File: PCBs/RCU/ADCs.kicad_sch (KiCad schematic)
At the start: 18 parts

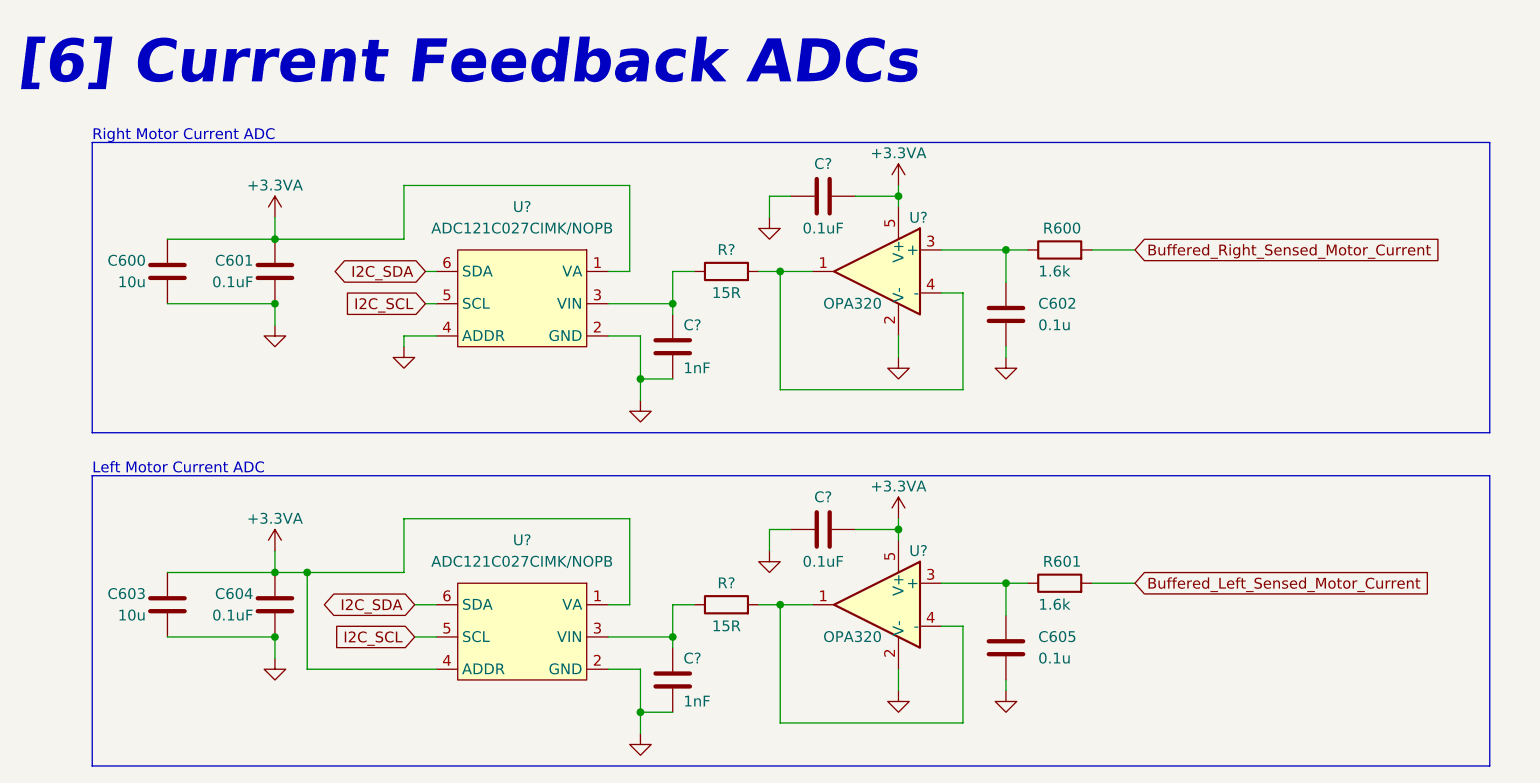
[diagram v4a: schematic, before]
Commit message: Fully annotated ADC schematic
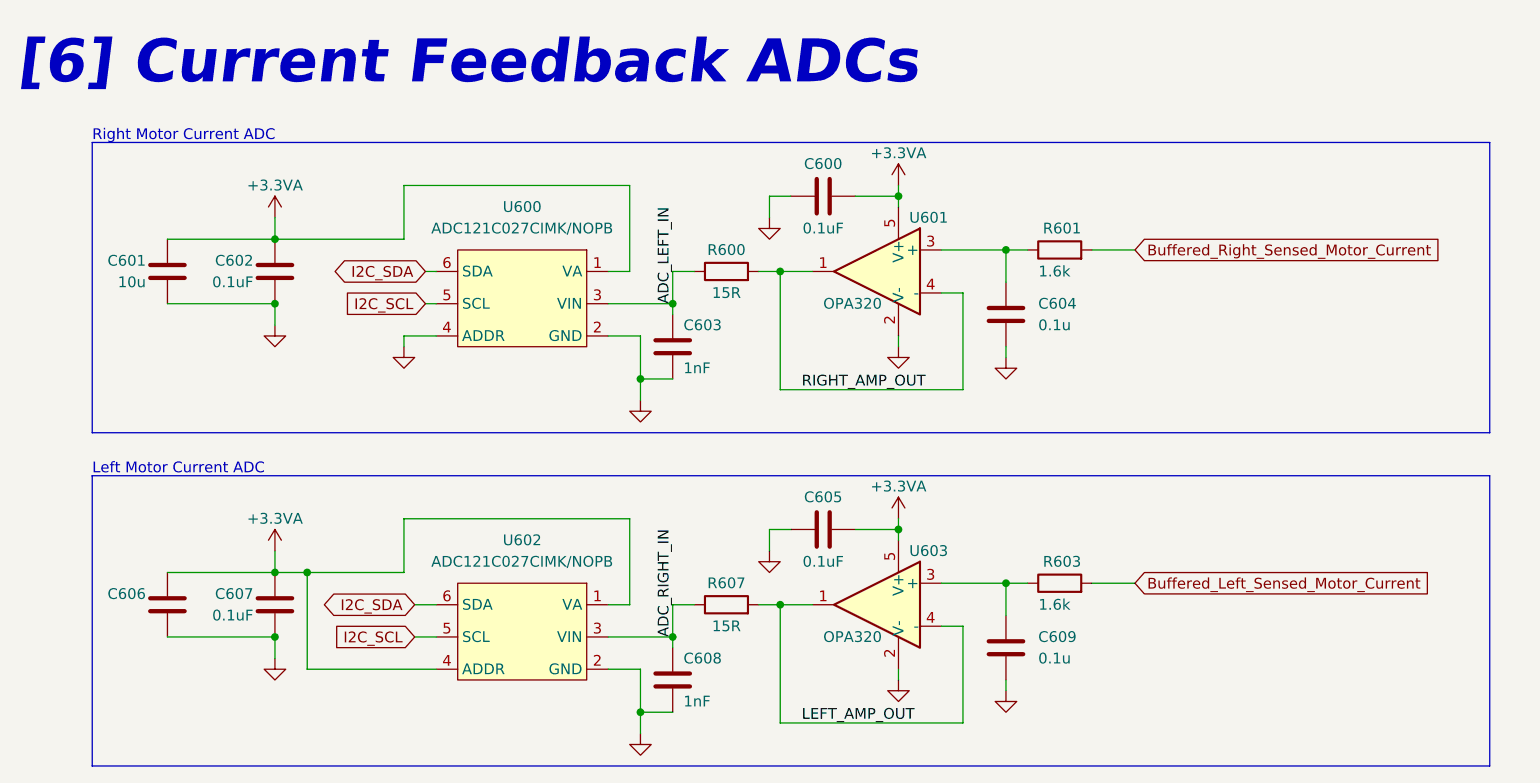
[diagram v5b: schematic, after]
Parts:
- C606: renamed from C603; value 10u -> (none)
- gave numbers to parts that had none: 10
- renumbered C600 to C601, C601 to C602, C602 to C604, C604 to C607, C605 to C609, R600 to R601, R601 to R603
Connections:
- net RIGHT_AMP_OUT: now reaches R600.2, U601.1, U601.4 (-)
- net ADC_RIGHT_IN: now reaches C608.1, R607.1, U602.3 (VIN)
- net ADC_LEFT_IN: now reaches C603.1, R600.1, U600.3 (VIN)
- net LEFT_AMP_OUT: now reaches R607.2, U603.1, U603.4 (-)
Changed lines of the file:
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@@
   (junction (at 105.41 83.82) (diameter 0) (color 0 0 0 0)
   )
-  (wire (pts (xy 119.38 91.44) (xy 119.38 93.98))
+  (wire (pts (xy 119.38 91.44) (xy 119.38 92.71))
     (stroke (width 0) (type default) (color 0 0 0 0))
   )
@@
     (stroke (width 0) (type default) (color 0 0 0 0))
   )
-  (wire (pts (xy 119.38 52.07) (xy 119.38 54.61))
+  (wire (pts (xy 119.38 52.07) (xy 119.38 53.34))
     (stroke (width 0) (type default) (color 0 0 0 0))
   )
@@
   (text "[6] Current Feedback ADCs" (at 15.24 22.86 0)
     (effects (font (size 5.08 5.08) (thickness 1.016) bold italic) (justify left bottom))
+  )
+  (label "LEFT_AMP_OUT" (at 107.95 97.79 0)
+    (effects (font (size 1.27 1.27)) (justify left bottom))
+  )
+  (label "RIGHT_AMP_OUT" (at 107.95 58.42 0)
+    (effects (font (size 1.27 1.27)) (justify left bottom))
+  )
+  (label "ADC_RIGHT_IN" (at 92.71 87.63 90)
+    (effects (font (size 1.27 1.27)) (justify left bottom))
+  )
+  (label "ADC_LEFT_IN" (at 92.71 48.26 90)
+    (effects (font (size 1.27 1.27)) (justify left bottom))
   )
   (global_label "I2C_SCL" (shape input) (at 63.5 48.26 180) (fields_autoplaced)
@@
     )
   )
-  (symbol (lib_id "power:GND") (at 119.38 93.98 0) (unit 1)
-    (in_bom yes) (on_board yes) (fields_autoplaced)
-    (property "Reference" "#PWR?" (id 0) (at 119.38 100.33 0)
-      (effects (font (size 1.27 1.27)) hide)
-    )
-    (property "Value" "GND" (id 1) (at 119.38 99.06 0)
-      (effects (font (size 1.27 1.27)) hide)
-    )
-    (property "Footprint" "" (id 2) (at 119.38 93.98 0)
-      (effects (font (size 1.27 1.27)) hide)
-    )
-    (property "Datasheet" "" (id 3) (at 119.38 93.98 0)
+  (symbol (lib_id "power:GND") (at 119.38 92.71 0) (unit 1)
+    (in_bom yes) (on_board yes) (fields_autoplaced)
+    (property "Reference" "#PWR?" (id 0) (at 119.38 99.06 0)
+      (effects (font (size 1.27 1.27)) hide)
+    )
+    (property "Value" "GND" (id 1) (at 119.38 97.79 0)
+      (effects (font (size 1.27 1.27)) hide)
+    )
+    (property "Footprint" "" (id 2) (at 119.38 92.71 0)
+      (effects (font (size 1.27 1.27)) hide)
+    )
+    (property "Datasheet" "" (id 3) (at 119.38 92.71 0)
       (effects (font (size 1.27 1.27)) hide)
     )
@@
   (symbol (lib_id "Device:R") (at 138.43 41.91 90) (unit 1)
     (in_bom yes) (on_board yes)
-    (property "Reference" "R600" (id 0) (at 140.97 39.37 90)
+    (property "Reference" "R601" (id 0) (at 140.97 39.37 90)
       (effects (font (size 1.27 1.27)) (justify left))
     )
@@
   (symbol (lib_id "Device:C") (at 45.72 44.45 0) (mirror y) (unit 1)
     (in_bom yes) (on_board yes)
-    (property "Reference" "C601" (id 0) (at 43.18 43.18 0)
+    (property "Reference" "C602" (id 0) (at 43.18 43.18 0)
       (effects (font (size 1.27 1.27)) (justify left))
     )
@@
   (symbol (lib_id "Device:C") (at 132.08 88.9 180) (unit 1)
     (in_bom yes) (on_board yes) (fields_autoplaced)
-    (property "Reference" "C605" (id 0) (at 135.89 87.6299 0)
+    (property "Reference" "C609" (id 0) (at 135.89 87.6299 0)
       (effects (font (size 1.27 1.27)) (justify right))
     )
@@
   (symbol (lib_id "Amplifier_Operational:OPA330xxDBV") (at 116.84 44.45 0) (mirror y) (unit 1)
     (in_bom yes) (on_board yes)
-    (property "Reference" "U?" (id 0) (at 120.65 38.1 0)
+    (property "Reference" "U601" (id 0) (at 120.65 38.1 0)
       (effects (font (size 1.27 1.27)) (justify right))
     )
@@
   (symbol (lib_id "Device:C") (at 110.49 35.56 90) (unit 1)
     (in_bom yes) (on_board yes)
-    (property "Reference" "C?" (id 0) (at 110.49 31.75 90))
+    (property "Reference" "C600" (id 0) (at 110.49 31.75 90))
     (property "Value" "0.1uF" (id 1) (at 110.49 39.37 90))
     (property "Footprint" "" (id 2) (at 114.3 34.5948 0)
@@
   (symbol (lib_id "Device:C") (at 110.49 74.93 90) (unit 1)
     (in_bom yes) (on_board yes)
-    (property "Reference" "C?" (id 0) (at 110.49 71.12 90))
+    (property "Reference" "C605" (id 0) (at 110.49 71.12 90))
     (property "Value" "0.1uF" (id 1) (at 110.49 78.74 90))
     (property "Footprint" "" (id 2) (at 114.3 73.9648 0)
@@
   (symbol (lib_id "Device:C") (at 33.02 44.45 0) (mirror y) (unit 1)
     (in_bom yes) (on_board yes)
-    (property "Reference" "C600" (id 0) (at 30.48 43.18 0)
+    (property "Reference" "C601" (id 0) (at 30.48 43.18 0)
       (effects (font (size 1.27 1.27)) (justify left))
     )
@@
   (symbol (lib_id "Device:C") (at 92.71 92.71 0) (unit 1)
     (in_bom yes) (on_board yes)
-    (property "Reference" "C?" (id 0) (at 93.98 90.17 0)
+    (property "Reference" "C608" (id 0) (at 93.98 90.17 0)
       (effects (font (size 1.27 1.27)) (justify left))
     )
@@
   (symbol (lib_id "Device:R") (at 99.06 44.45 90) (unit 1)
     (in_bom yes) (on_board yes)
-    (property "Reference" "R?" (id 0) (at 99.06 41.91 90))
+    (property "Reference" "R600" (id 0) (at 99.06 41.91 90))
     (property "Value" "15R" (id 1) (at 99.06 46.99 90))
     (property "Footprint" "" (id 2) (at 99.06 46.228 90)
@@
   (symbol (lib_id "Device:C") (at 92.71 53.34 0) (unit 1)
     (in_bom yes) (on_board yes)
-    (property "Reference" "C?" (id 0) (at 93.98 50.8 0)
+    (property "Reference" "C603" (id 0) (at 93.98 50.8 0)
       (effects (font (size 1.27 1.27)) (justify left))
     )
@@
   (symbol (lib_id "Device:C") (at 33.02 83.82 0) (mirror y) (unit 1)
     (in_bom yes) (on_board yes)
-    (property "Reference" "C603" (id 0) (at 30.48 82.55 0)
-      (effects (font (size 1.27 1.27)) (justify left))
-    )
-    (property "Value" "10u" (id 1) (at 30.48 85.09 0)
+    (property "Reference" "C606" (id 0) (at 30.48 82.55 0)
+      (effects (font (size 1.27 1.27)) (justify left))
+    )
+    (property "Value" "" (id 1) (at 30.48 85.09 0)
       (effects (font (size 1.27 1.27)) (justify left))
     )
@@
   (symbol (lib_id "Device:C") (at 45.72 83.82 0) (mirror y) (unit 1)
     (in_bom yes) (on_board yes)
-    (property "Reference" "C604" (id 0) (at 43.18 82.55 0)
+    (property "Reference" "C607" (id 0) (at 43.18 82.55 0)
       (effects (font (size 1.27 1.27)) (justify left))
     )
@@
     (pin "2")
   )
-  (symbol (lib_id "power:GND") (at 119.38 54.61 0) (unit 1)
-    (in_bom yes) (on_board yes) (fields_autoplaced)
-    (property "Reference" "#PWR?" (id 0) (at 119.38 60.96 0)
-      (effects (font (size 1.27 1.27)) hide)
-    )
-    (property "Value" "GND" (id 1) (at 119.38 59.69 0)
-      (effects (font (size 1.27 1.27)) hide)
-    )
-    (property "Footprint" "" (id 2) (at 119.38 54.61 0)
-      (effects (font (size 1.27 1.27)) hide)
-    )
-    (property "Datasheet" "" (id 3) (at 119.38 54.61 0)
+  (symbol (lib_id "power:GND") (at 119.38 53.34 0) (unit 1)
+    (in_bom yes) (on_board yes) (fields_autoplaced)
+    (property "Reference" "#PWR?" (id 0) (at 119.38 59.69 0)
+      (effects (font (size 1.27 1.27)) hide)
+    )
+    (property "Value" "GND" (id 1) (at 119.38 58.42 0)
+      (effects (font (size 1.27 1.27)) hide)
+    )
+    (property "Footprint" "" (id 2) (at 119.38 53.34 0)
+      (effects (font (size 1.27 1.27)) hide)
+    )
+    (property "Datasheet" "" (id 3) (at 119.38 53.34 0)
       (effects (font (size 1.27 1.27)) hide)
     )
@@
   (symbol (lib_id "Device:R") (at 138.43 81.28 90) (unit 1)
     (in_bom yes) (on_board yes)
-    (property "Reference" "R601" (id 0) (at 140.97 78.74 90)
+    (property "Reference" "R603" (id 0) (at 140.97 78.74 90)
       (effects (font (size 1.27 1.27)) (justify left))
     )
@@
   (symbol (lib_name "ADC121C027CIMK{slash}NOPB_1") (lib_id "Ghanis_Symbols_KiCad6:ADC121C027CIMK{slash}NOPB") (at 74.93 40.64 0) (mirror y) (unit 1)
     (in_bom yes) (on_board yes) (fields_autoplaced)
-    (property "Reference" "U?" (id 0) (at 74.93 36.83 0))
+    (property "Reference" "U600" (id 0) (at 74.93 36.83 0))
     (property "Value" "ADC121C027CIMK/NOPB" (id 1) (at 74.93 39.37 0))
     (property "Footprint" "" (id 2) (at 85.09 38.1 0)
@@
   (symbol (lib_id "Amplifier_Operational:OPA330xxDBV") (at 116.84 83.82 0) (mirror y) (unit 1)
     (in_bom yes) (on_board yes)
-    (property "Reference" "U?" (id 0) (at 120.65 77.47 0)
+    (property "Reference" "U603" (id 0) (at 120.65 77.47 0)
       (effects (font (size 1.27 1.27)) (justify right))
     )
@@
   (symbol (lib_id "Device:C") (at 132.08 49.53 180) (unit 1)
     (in_bom yes) (on_board yes) (fields_autoplaced)
-    (property "Reference" "C602" (id 0) (at 135.89 48.2599 0)
+    (property "Reference" "C604" (id 0) (at 135.89 48.2599 0)
       (effects (font (size 1.27 1.27)) (justify right))
     )
@@
   (symbol (lib_id "Device:R") (at 99.06 83.82 90) (unit 1)
     (in_bom yes) (on_board yes)
-    (property "Reference" "R?" (id 0) (at 99.06 81.28 90))
+    (property "Reference" "R607" (id 0) (at 99.06 81.28 90))
     (property "Value" "15R" (id 1) (at 99.06 86.36 90))
     (property "Footprint" "" (id 2) (at 99.06 85.598 90)
@@
   (symbol (lib_name "ADC121C027CIMK{slash}NOPB_1") (lib_id "Ghanis_Symbols_KiCad6:ADC121C027CIMK{slash}NOPB") (at 74.93 80.01 0) (mirror y) (unit 1)
     (in_bom yes) (on_board yes) (fields_autoplaced)
-    (property "Reference" "U?" (id 0) (at 74.93 76.2 0))
+    (property "Reference" "U602" (id 0) (at 74.93 76.2 0))
     (property "Value" "ADC121C027CIMK/NOPB" (id 1) (at 74.93 78.74 0))
     (property "Footprint" "" (id 2) (at 85.09 77.47 0)

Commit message: Schematic cleanup
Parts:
- C601: value 10u -> (none)
- C604, C609: value 0.1u -> (none)
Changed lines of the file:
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@@
       (effects (font (size 1.27 1.27)) (justify right))
     )
-    (property "Value" "0.1u" (id 1) (at 135.89 90.1699 0)
+    (property "Value" "" (id 1) (at 135.89 90.1699 0)
       (effects (font (size 1.27 1.27)) (justify right))
     )
@@
       (effects (font (size 1.27 1.27)) (justify left))
     )
-    (property "Value" "10u" (id 1) (at 30.48 45.72 0)
+    (property "Value" "" (id 1) (at 30.48 45.72 0)
       (effects (font (size 1.27 1.27)) (justify left))
     )
@@
       (effects (font (size 1.27 1.27)) (justify right))
     )
-    (property "Value" "0.1u" (id 1) (at 135.89 50.7999 0)
-      (effects (font (size 1.27 1.27)) (justify right))
-    )
+    (property "Value" "" (id 1) (at 135.89 50.7999 0)
+      (effects (font (size 1.27 1.27)) (justify right))
+    )

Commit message: Corrected SPI_MOSI and SPI_MISO labels on U700 - external memory
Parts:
- C601, C606: value (none) -> 10uF
- C604, C609: value (none) -> 0.1uF
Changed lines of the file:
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@@
       (effects (font (size 1.27 1.27)) (justify right))
     )
-    (property "Value" "" (id 1) (at 135.89 90.1699 0)
+    (property "Value" "0.1uF" (id 1) (at 135.89 90.1699 0)
       (effects (font (size 1.27 1.27)) (justify right))
     )
@@
       (effects (font (size 1.27 1.27)) (justify left))
     )
-    (property "Value" "" (id 1) (at 30.48 45.72 0)
+    (property "Value" "10uF" (id 1) (at 30.48 45.72 0)
       (effects (font (size 1.27 1.27)) (justify left))
     )
@@
       (effects (font (size 1.27 1.27)) (justify left))
     )
-    (property "Value" "" (id 1) (at 30.48 85.09 0)
+    (property "Value" "10uF" (id 1) (at 30.48 85.09 0)
       (effects (font (size 1.27 1.27)) (justify left))
     )
@@
       (effects (font (size 1.27 1.27)) (justify right))
     )
-    (property "Value" "" (id 1) (at 135.89 50.7999 0)
-      (effects (font (size 1.27 1.27)) (justify right))
-    )
+    (property "Value" "0.1uF" (id 1) (at 135.89 50.7999 0)
+      (effects (font (size 1.27 1.27)) (justify right))
+    )

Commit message: Change address pin of left motor ADC to floating so that it and the light sensor will have diffeent addresses, wrote slave addresses for ADCs and light sensor
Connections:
- net +3.3VA: no longer U602.4 (ADDR)
- no-connect marks 0 -> 1
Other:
- note added: "Slave Address: 1010000"
- note added: "Slave Address: 1010001"
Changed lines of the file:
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@@
   (junction (at 88.9 96.52) (diameter 0) (color 0 0 0 0)
   )
-  (junction (at 49.53 80.01) (diameter 0) (color 0 0 0 0)
-  )
   (junction (at 119.38 35.56) (diameter 0) (color 0 0 0 0)
   )
@@
   (junction (at 105.41 83.82) (diameter 0) (color 0 0 0 0)
   )
+  (no_connect (at 64.77 91.44))
   (wire (pts (xy 119.38 91.44) (xy 119.38 92.71))
     (stroke (width 0) (type default) (color 0 0 0 0))
@@
     (stroke (width 0) (type default) (color 0 0 0 0))
   )
-  (wire (pts (xy 60.96 80.01) (xy 49.53 80.01))
-    (stroke (width 0) (type default) (color 0 0 0 0))
-  )
   (wire (pts (xy 104.14 74.93) (xy 104.14 77.47))
     (stroke (width 0) (type default) (color 0 0 0 0))
@@
     (stroke (width 0) (type default) (color 0 0 0 0))
   )
-  (wire (pts (xy 64.77 91.44) (xy 49.53 91.44))
-    (stroke (width 0) (type default) (color 0 0 0 0))
-  )
   (wire (pts (xy 88.9 57.15) (xy 88.9 59.69))
     (stroke (width 0) (type default) (color 0 0 0 0))
@@
     (stroke (width 0) (type default) (color 0 0 0 0))
   )
-  (wire (pts (xy 49.53 91.44) (xy 49.53 80.01))
-    (stroke (width 0) (type default) (color 0 0 0 0))
-  )
   (wire (pts (xy 105.41 58.42) (xy 105.41 44.45))
     (stroke (width 0) (type default) (color 0 0 0 0))
@@
     (stroke (width 0) (type default) (color 0 0 0 0))
   )
-  (wire (pts (xy 49.53 80.01) (xy 45.72 80.01))
+  (wire (pts (xy 45.72 80.01) (xy 60.96 80.01))
     (stroke (width 0) (type default) (color 0 0 0 0))
   )
@@
   )
   (text "Left Motor Current ADC" (at 24.13 68.58 0)
+    (effects (font (size 1.27 1.27)) (justify left bottom))
+  )
+  (text "Slave Address: 1010001" (at 63.5 55.88 0)
     (effects (font (size 1.27 1.27)) (justify left bottom))
   )
@@
     (effects (font (size 5.08 5.08) (thickness 1.016) bold italic) (justify left bottom))
   )
+  (text "Slave Address: 1010000" (at 63.5 95.25 0)
+    (effects (font (size 1.27 1.27)) (justify left bottom))
+  )
   (label "LEFT_AMP_OUT" (at 107.95 97.79 0)
